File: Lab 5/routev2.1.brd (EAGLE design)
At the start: 100 x 80 mm, 48 parts, among them J1 FTDI_DEVICERA_SMT, M1 WIRELESS-NRF24L01, U1 3.3V, U2 GY-521MPU6050

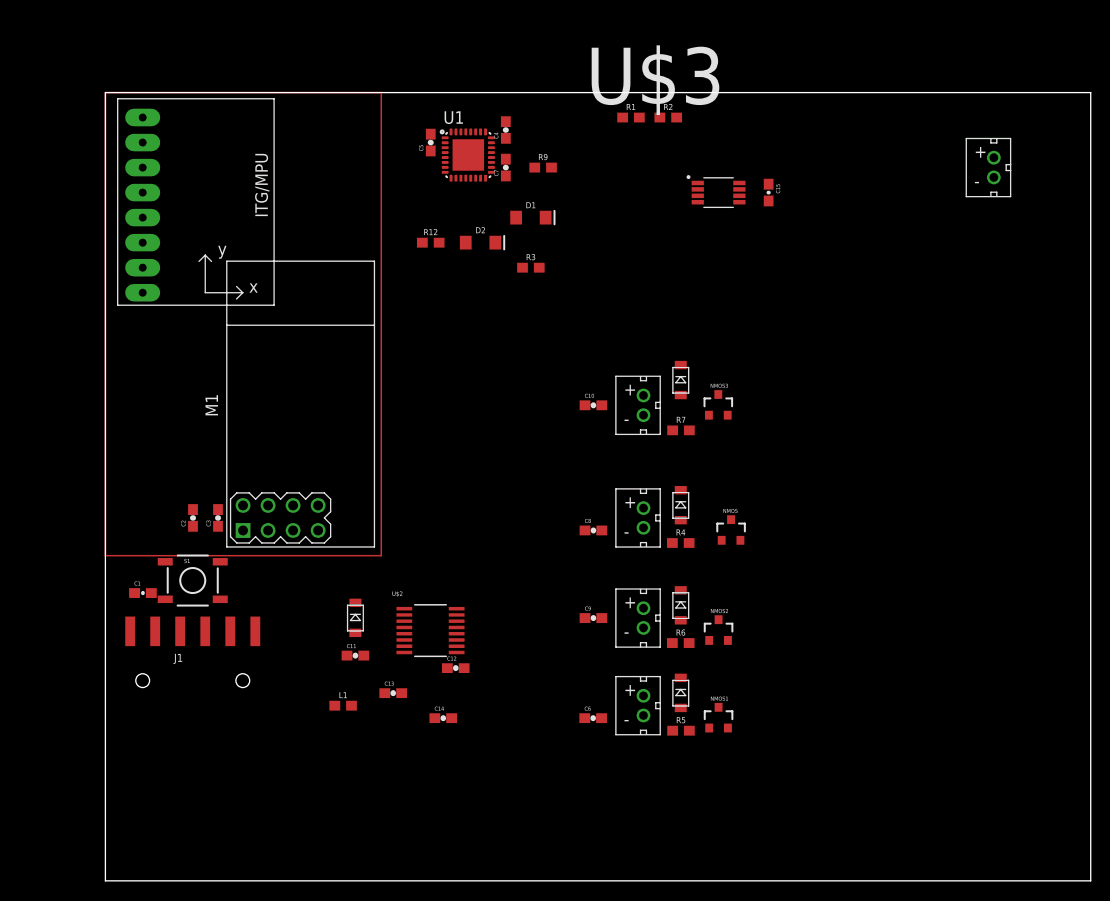
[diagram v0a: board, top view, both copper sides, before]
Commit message: Check routev2.3.brd for one with no error
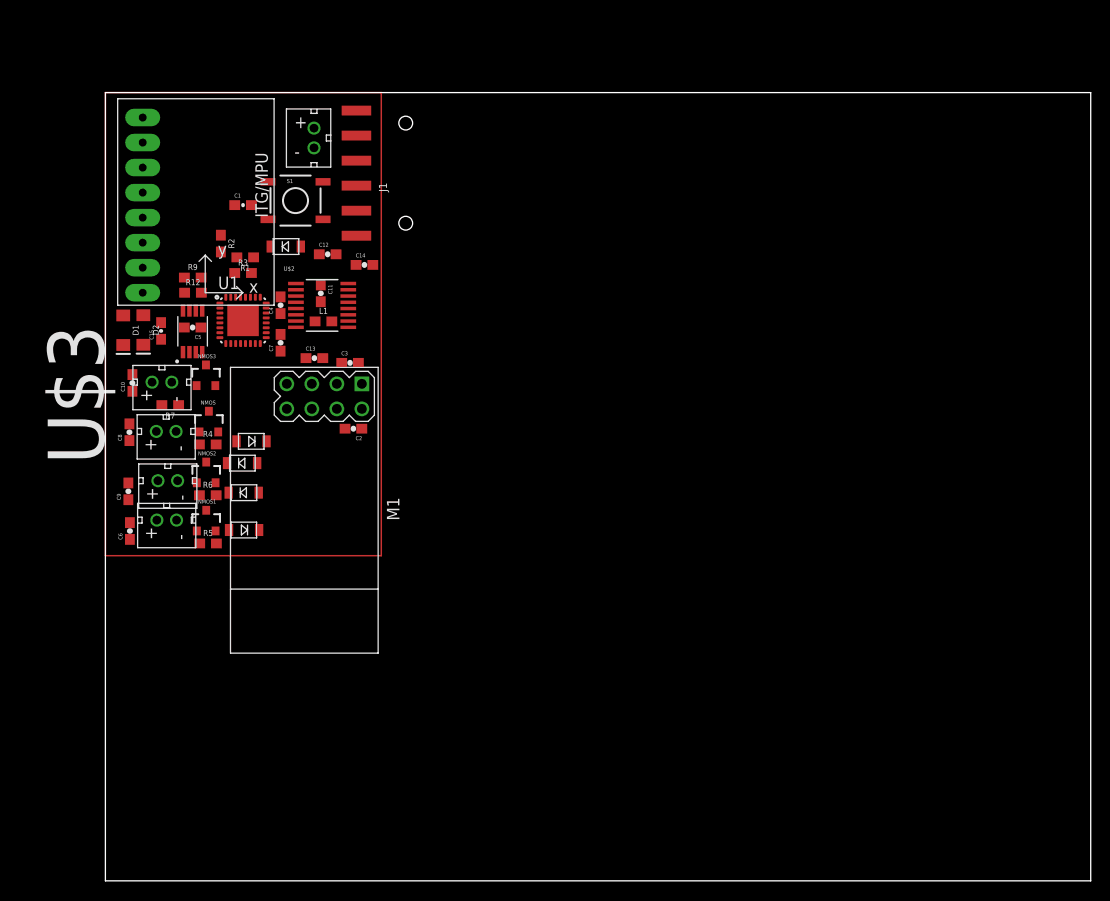
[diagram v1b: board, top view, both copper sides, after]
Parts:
- moved U$1 69.1 mm to (21.2, 75.4)
- moved C15 63.2 mm to (5.65, 55.8), turned to 90 degrees
- moved J1 55.9 mm to (30.5, 71.8), turned to 90 degrees
- moved NMOS1 55.7 mm to (10.2, 36.5)
- moved U$3 55.2 mm to (8.85, 55.8), turned to 90 degrees
- moved NMOS2 54.4 mm to (10.2, 41.4)
- moved NMOS 54.1 mm to (10.5, 46.6)
- moved NMOS3 52.1 mm to (10.2, 51.3)
- moved MOTOR1 51.9 mm to (6.22, 36.6), turned to 90 degrees
- moved R7 51.9 mm to (6.58, 48.3), turned to 180 degrees
- moved R5 51.6 mm to (10.4, 34.2)
- moved C6 50.7 mm to (2.49, 35.5), turned to 90 degrees
- moved R6 50.3 mm to (10.4, 39.1)
- moved MOTOR2 50.3 mm to (6.33, 40.6), turned to 90 degrees
- moved MOTOR 49.2 mm to (6.17, 45.6), turned to 90 degrees
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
